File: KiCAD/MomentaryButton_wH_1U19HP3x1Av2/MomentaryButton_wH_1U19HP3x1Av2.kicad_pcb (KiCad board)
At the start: 2 copper layers, 96.3 x 39.7 mm, 8 parts, among them SW1 SW_SPST_M16_Panel_Mount_Push-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, SW2 SW_SPST_M16_Panel_Mount_Push-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, SW3 SW_SPST_M16_Panel_Mount_Push-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

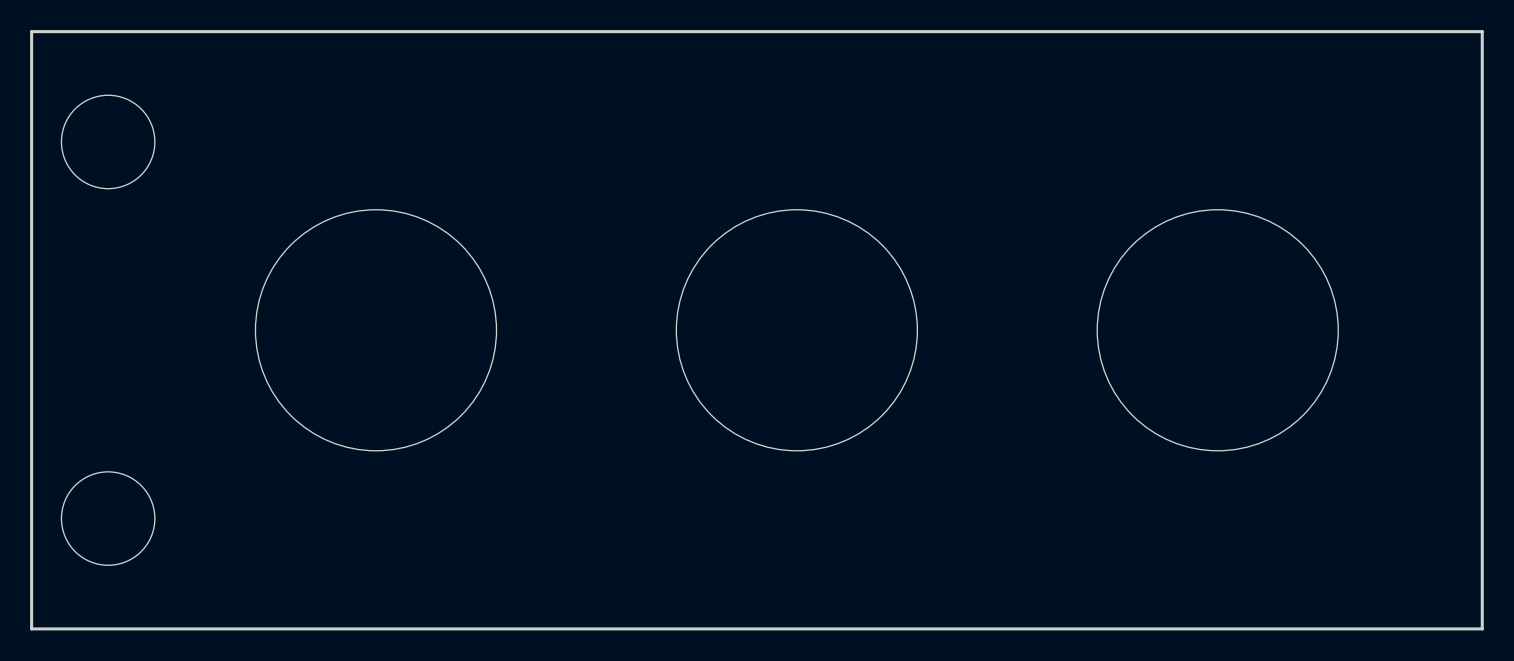
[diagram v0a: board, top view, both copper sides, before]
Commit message: updated all modules to use plated through-holes wherever possible
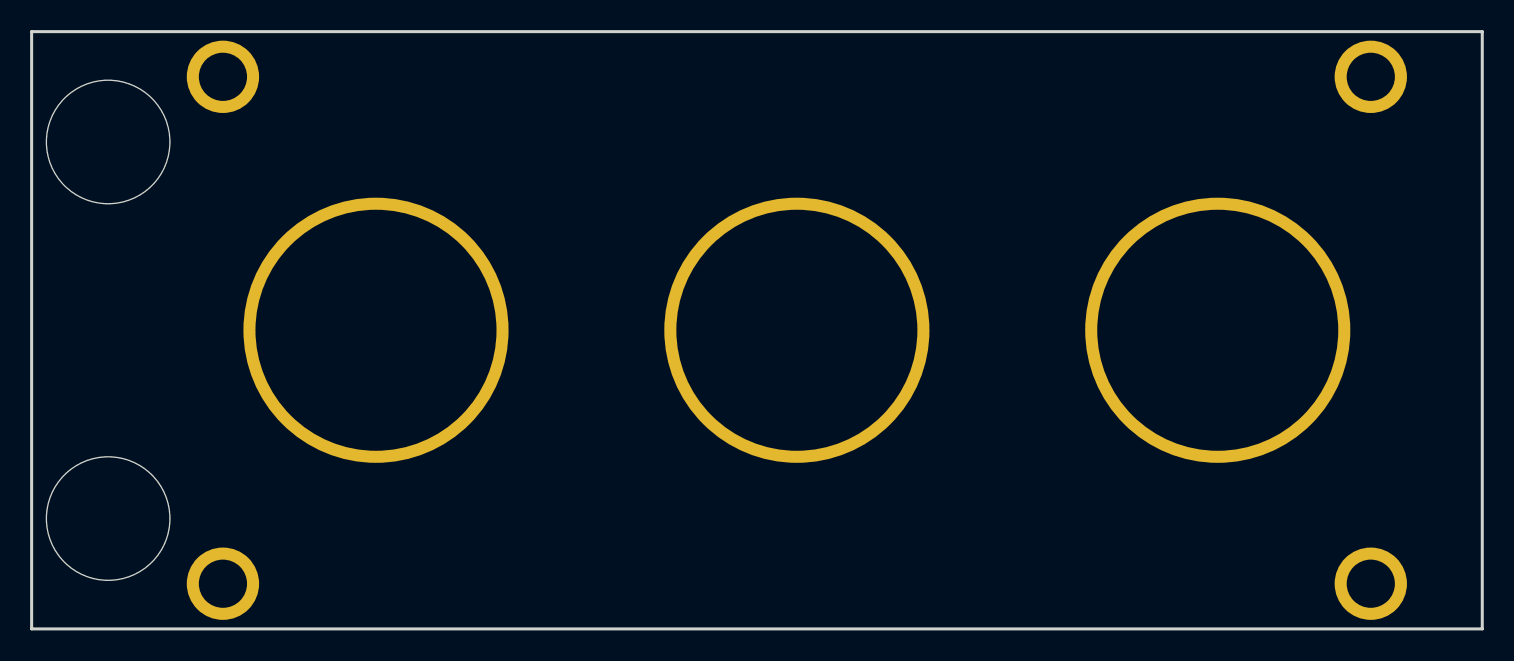
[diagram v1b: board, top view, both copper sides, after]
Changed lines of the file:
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@@
 			)
 		)
-		(pad "" np_thru_hole circle
+		(pad "" thru_hole circle
 			(at 0 0)
-			(size 16 16)
+			(size 17.6 17.6)
 			(drill 16)
 			(layers "*.Cu" "*.Mask")
+			(remove_unused_layers no)
 		)
 		(embedded_fonts no)
@@
 			)
 		)
-		(pad "" np_thru_hole circle
+		(pad "" thru_hole circle
 			(at 0 0)
-			(size 16 16)
+			(size 17.6 17.6)
 			(drill 16)
 			(layers "*.Cu" "*.Mask")
+			(remove_unused_layers no)
 		)
 		(embedded_fonts no)
@@
 			)
 		)
-		(pad "" np_thru_hole oval
+		(pad "" thru_hole circle
 			(at 0 0)
-			(size 4.34 3.2)
-			(drill oval 4.34 3.2)
-			(layers "*.Cu" "*.Mask")
+			(size 4.8 4.8)
+			(drill 3.2)
+			(layers "*.Cu" "*.Mask")
+			(remove_unused_layers no)
 		)
 		(embedded_fonts no)
@@
 			)
 		)
-		(pad "" np_thru_hole oval
+		(pad "" thru_hole circle
 			(at 0 0)
-			(size 4.34 3.2)
-			(drill oval 4.34 3.2)
-			(layers "*.Cu" "*.Mask")
+			(size 4.8 4.8)
+			(drill 3.2)
+			(layers "*.Cu" "*.Mask")
+			(remove_unused_layers no)
 		)
 		(embedded_fonts no)
@@
 			)
 		)
-		(pad "" np_thru_hole circle
+		(pad "" thru_hole circle
 			(at 0 0)
-			(size 16 16)
+			(size 17.6 17.6)
 			(drill 16)
 			(layers "*.Cu" "*.Mask")
+			(remove_unused_layers no)
 		)
 		(embedded_fonts no)
@@
 			)
 		)
-		(pad "" np_thru_hole oval
+		(pad "" thru_hole circle
 			(at 0 0)
-			(size 4.34 3.2)
-			(drill oval 4.34 3.2)
-			(layers "*.Cu" "*.Mask")
+			(size 4.8 4.8)
+			(drill 3.2)
+			(layers "*.Cu" "*.Mask")
+			(remove_unused_layers no)
 		)
 		(embedded_fonts no)
@@
 			)
 		)
-		(pad "" np_thru_hole oval
+		(pad "" thru_hole circle
 			(at 0 0)
-			(size 4.34 3.2)
-			(drill oval 4.34 3.2)
-			(layers "*.Cu" "*.Mask")
+			(size 4.8 4.8)
+			(drill 3.2)
+			(layers "*.Cu" "*.Mask")
+			(remove_unused_layers no)
 		)
 		(embedded_fonts no)
@@
 		(at 5.08 9.75)
 		(property "Reference" "H5"
-			(at 0 -4 0)
+			(at -0.08 -5 0)
 			(unlocked yes)
 			(layer "B.SilkS")
@@
 					(size 1 1)
 					(thickness 0.15)
+				)
+			)
+		)
+		(property "Source" "https://www.aliexpress.com/item/1005005070119421.html"
+			(at 0 36.25 0)
+			(layer "F.Fab")
+			(hide yes)
+			(effects
+				(font
+					(size 1 1)
+					(thickness 0.1)
 				)
 			)
@@
 		(fp_circle
 			(center 0 0)
-			(end 3.1 0)
+			(end 4.1 0)
 			(stroke
 				(width 0.2)
@@
 		(fp_circle
 			(center 0 25)
-			(end 3.1 25)
+			(end 4.1 25)
 			(stroke
 				(width 0.2)
@@
 		(pad "" np_thru_hole circle
 			(at 0 0)
-			(size 6.2 6.2)
-			(drill 6.2)
+			(size 8.2 8.2)
+			(drill 8.2)
 			(layers "*.Cu" "*.Mask")
 		)
 		(pad "" np_thru_hole circle
 			(at 0 25)
-			(size 6.2 6.2)
-			(drill 6.2)
-			(layers "*.Cu" "*.Mask")
-		)
+			(size 8.2 8.2)
+			(drill 8.2)
+			(layers "*.Cu" "*.Mask")
+		)
